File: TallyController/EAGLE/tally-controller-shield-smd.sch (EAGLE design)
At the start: 28 parts, among them J2 Mega R3, U1 SN75174N, U2 SN75174N, U3 SN75174N

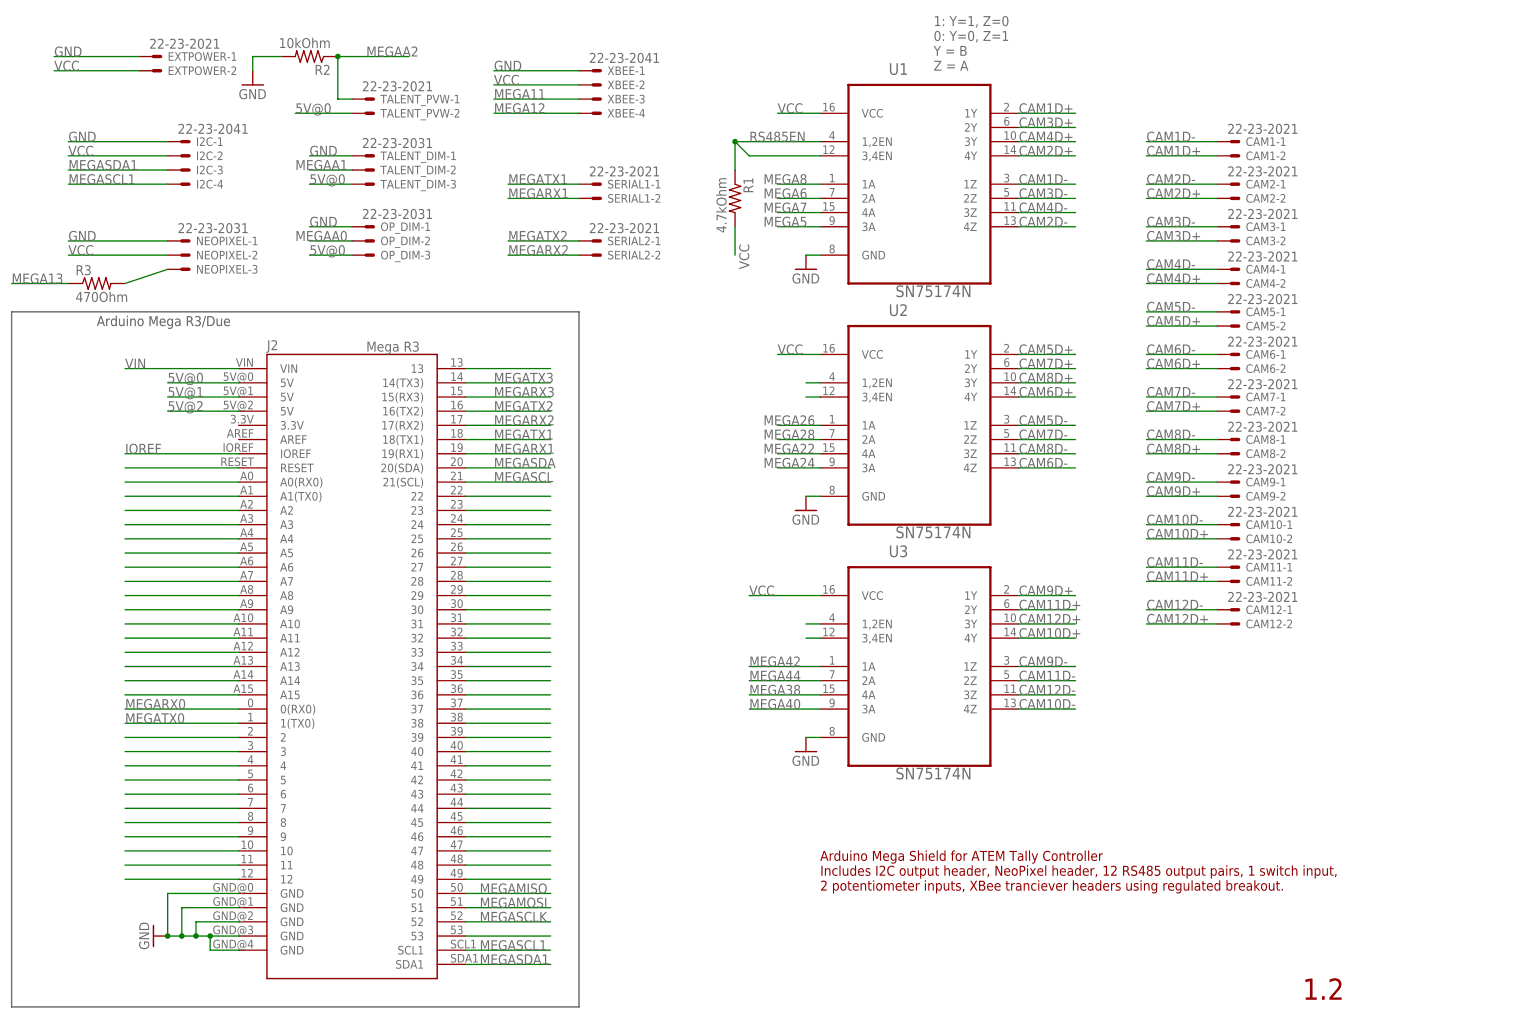
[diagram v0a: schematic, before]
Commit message: Go through and fix notation on RS485 wiring everywhere to use the standard A/B notation.
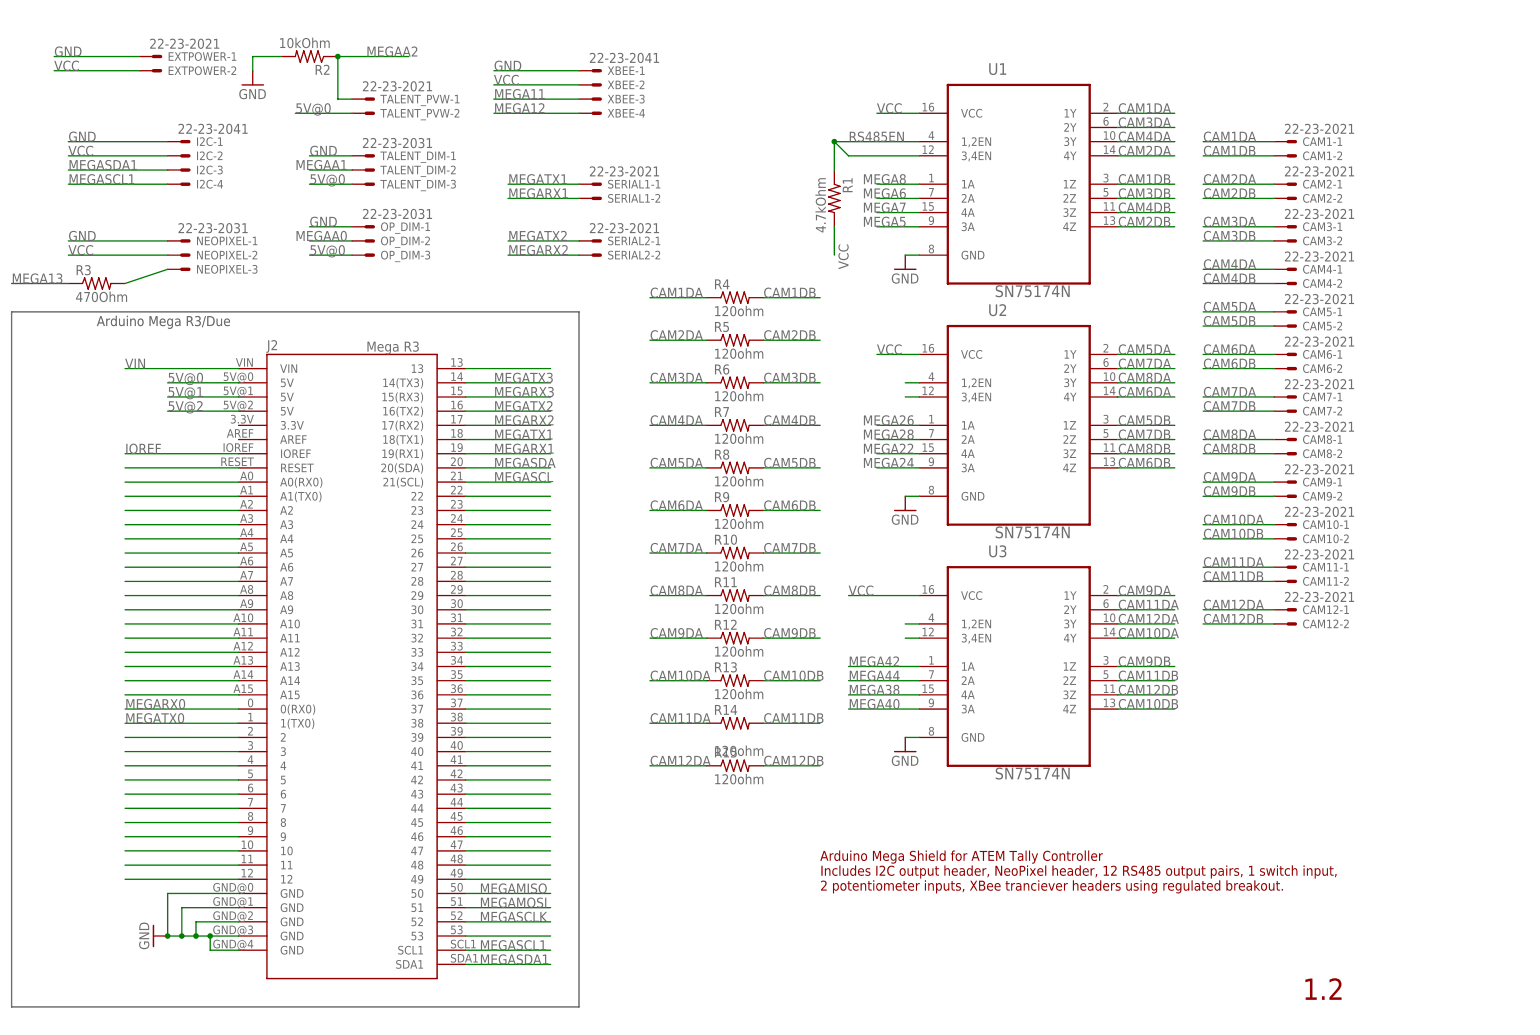
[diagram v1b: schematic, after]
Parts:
- added R10, R11, R12, R13, R14, R15, R4, R5, R6, R7, R8, R9: 120ohm, rcl:R-US_R0805
- R1, R2, R3: device rcl:R-US_R1206 -> rcl:R-US_R0805
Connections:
- removed net CAM10D+: CAM10-2.S, U3.4Y
- removed net CAM10D-: CAM10-1.S, U3.4Z
- removed net CAM11D+: CAM11-2.S, U3.2Y
- removed net CAM11D-: CAM11-1.S, U3.2Z
- removed net CAM12D+: CAM12-2.S, U3.3Y
- removed net CAM12D-: CAM12-1.S, U3.3Z
- removed net CAM1D+: CAM1-2.S, U1.1Y
- removed net CAM1D-: CAM1-1.S, U1.1Z
- removed net CAM2D+: CAM2-2.S, U1.4Y
- removed net CAM2D-: CAM2-1.S, U1.4Z
- removed net CAM3D+: CAM3-2.S, U1.2Y
- removed net CAM3D-: CAM3-1.S, U1.2Z
- removed net CAM4D+: CAM4-2.S, U1.3Y
- removed net CAM4D-: CAM4-1.S, U1.3Z
- removed net CAM5D+: CAM5-2.S, U2.1Y
- removed net CAM5D-: CAM5-1.S, U2.1Z
- removed net CAM6D+: CAM6-2.S, U2.4Y
- removed net CAM6D-: CAM6-1.S, U2.4Z
- removed net CAM7D+: CAM7-2.S, U2.2Y
- removed net CAM7D-: CAM7-1.S, U2.2Z
- removed net CAM8D+: CAM8-2.S, U2.3Y
- removed net CAM8D-: CAM8-1.S, U2.3Z
- removed net CAM9D+: CAM9-2.S, U3.1Y
- removed net CAM9D-: CAM9-1.S, U3.1Z
- new net CAM10DA: CAM10-1.S, R13.1, U3.4Y
- new net CAM10DB: CAM10-2.S, R13.2, U3.4Z
- new net CAM11DA: CAM11-1.S, R14.1, U3.2Y
- new net CAM11DB: CAM11-2.S, R14.2, U3.2Z
- new net CAM12DA: CAM12-1.S, R15.1, U3.3Y
- new net CAM12DB: CAM12-2.S, R15.2, U3.3Z
- new net CAM1DA: CAM1-1.S, R4.1, U1.1Y
- new net CAM1DB: CAM1-2.S, R4.2, U1.1Z
- new net CAM2DA: CAM2-1.S, R5.1, U1.4Y
- new net CAM2DB: CAM2-2.S, R5.2, U1.4Z
- new net CAM3DA: CAM3-1.S, R6.1, U1.2Y
- new net CAM3DB: CAM3-2.S, R6.2, U1.2Z
- new net CAM4DA: CAM4-1.S, R7.1, U1.3Y
- new net CAM4DB: CAM4-2.S, R7.2, U1.3Z
- new net CAM5DA: CAM5-1.S, R8.1, U2.1Y
- new net CAM5DB: CAM5-2.S, R8.2, U2.1Z
- new net CAM6DA: CAM6-1.S, R9.1, U2.4Y
- new net CAM6DB: CAM6-2.S, R9.2, U2.4Z
- new net CAM7DA: CAM7-1.S, R10.1, U2.2Y
- new net CAM7DB: CAM7-2.S, R10.2, U2.2Z
- new net CAM8DA: CAM8-1.S, R11.1, U2.3Y
- new net CAM8DB: CAM8-2.S, R11.2, U2.3Z
- new net CAM9DA: CAM9-1.S, R12.1, U3.1Y
- new net CAM9DB: CAM9-2.S, R12.2, U3.1Z
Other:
- note removed: "1: Y=1, Z=0 0: Y=0, Z=1 Y = B Z = A"
- moved on the sheet: CAM1-1, CAM1-2, CAM10-1, CAM10-2, CAM11-1, CAM11-2, CAM12-1, CAM12-2, CAM2-1, CAM2-2, CAM3-1, CAM3-2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

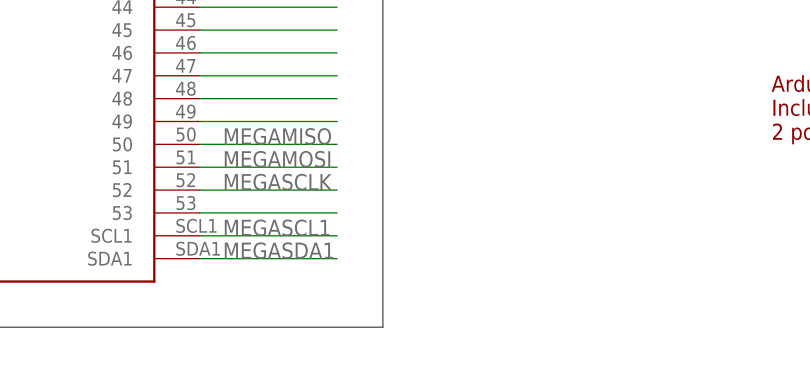
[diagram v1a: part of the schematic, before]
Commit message: Revisions to SMD version of controller board.  Create board for wireless tally.  Code revisions to sketch.
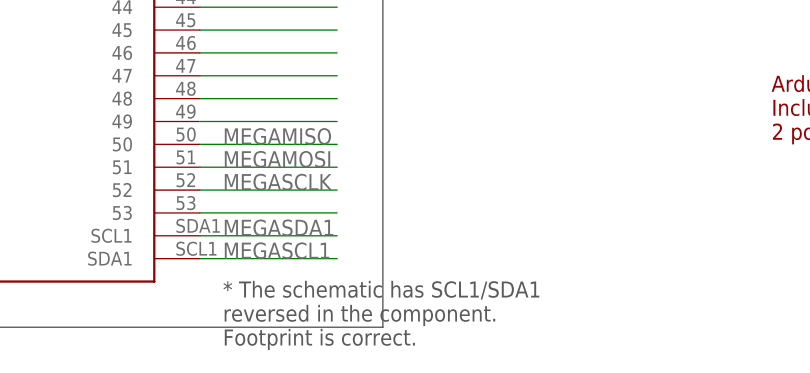
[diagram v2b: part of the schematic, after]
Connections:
- net MEGASCL1: now also J2.SDA1; no longer J2.SCL1
- net MEGASDA1: now also J2.SCL1; no longer J2.SDA1
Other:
- note added: "* The schematic has SCL1/SDA1 reversed in the component. Footprint is correct."
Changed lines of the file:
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@@
 2 potentiometer inputs, XBee tranciever headers using regulated breakout.</text>
 <text x="71.12" y="-7.62" size="3.81" layer="94" align="top-left">1.2</text>
+<text x="-76.2" y="-7.62" size="1.778" layer="97" align="top-left">* The schematic has SCL1/SDA1
+reversed in the component.
+Footprint is correct.</text>
 </plain>
 <instances>
@@
 <net name="MEGASDA1" class="0">
 <segment>
+<wire x1="-132.08" y1="137.16" x2="-149.86" y2="137.16" width="0.1524" layer="91"/>
+<label x="-149.86" y="137.16" size="1.778" layer="95"/>
+<pinref part="I2C" gate="-3" pin="S"/>
+</segment>
+<segment>
+<pinref part="J2" gate="G$1" pin="SCL1"/>
+<wire x1="-78.74" y1="-2.54" x2="-63.5" y2="-2.54" width="0.1524" layer="91"/>
+<label x="-76.2" y="-2.54" size="1.778" layer="95"/>
+</segment>
+</net>
+<net name="MEGASCL1" class="0">
+<segment>
+<wire x1="-132.08" y1="134.62" x2="-149.86" y2="134.62" width="0.1524" layer="91"/>
+<label x="-149.86" y="134.62" size="1.778" layer="95"/>
+<pinref part="I2C" gate="-4" pin="S"/>
+</segment>
+<segment>
 <pinref part="J2" gate="G$1" pin="SDA1"/>
 <wire x1="-78.74" y1="-5.08" x2="-63.5" y2="-5.08" width="0.1524" layer="91"/>
 <label x="-76.2" y="-5.08" size="1.778" layer="95"/>
 </segment>
-<segment>
-<wire x1="-132.08" y1="137.16" x2="-149.86" y2="137.16" width="0.1524" layer="91"/>
-<label x="-149.86" y="137.16" size="1.778" layer="95"/>
-<pinref part="I2C" gate="-3" pin="S"/>
-</segment>
-</net>
-<net name="MEGASCL1" class="0">
-<segment>
-<pinref part="J2" gate="G$1" pin="SCL1"/>
-<wire x1="-78.74" y1="-2.54" x2="-63.5" y2="-2.54" width="0.1524" layer="91"/>
-<label x="-76.2" y="-2.54" size="1.778" layer="95"/>
-</segment>
-<segment>
-<wire x1="-132.08" y1="134.62" x2="-149.86" y2="134.62" width="0.1524" layer="91"/>
-<label x="-149.86" y="134.62" size="1.778" layer="95"/>
-<pinref part="I2C" gate="-4" pin="S"/>
-</segment>
-</net>
+</net>
